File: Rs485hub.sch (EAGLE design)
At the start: 97 parts, among them IC1 SN75176PA, IC2 74AC00N, IC3 SN75176PA, IC4 74AC00N, IC5 SN75176PA, IC6 74AC00N, IC7 SN75176PA, IC8 74AC00N

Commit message: Further mods for the 19" rack at RaumZeitLabor, still needs routing
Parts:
- removed J1, J2, J3, J4: (no value), con-amp:557786-1
- removed RXD1, RXD2, RXD3, RXD4: Grn rxd, led:LED3MM
- removed TXD1, TXD2, TXD3, TXD4: red txd, led:LED3MM
- added U$2, U$3, U$4, U$5: RJHS508, RJHS:RJHS508
- added X1: MAB64, con-vg:MAB64
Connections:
- net GND: now also U$2G$2.PK$1, U$2G$3.PK$1, U$3G$2.PK$1, U$3G$3.PK$1, U$4G$2.PK$1, U$4G$3.PK$1, U$5G$2.PK$1, U$5G$3.PK$1, X1A.29; no longer RXD1.C, RXD2.C, RXD3.C, RXD4.C, TXD1.C, TXD2.C, TXD3.C, TXD4.C
- net N$1: now also U$2G$3.PA$1; no longer TXD1.A
- net N$10: now also U$2G$1.P$1; no longer J2.1
- net N$17: now also U$3G$2.PA$1; no longer RXD2.A
- net N$18: now also U$3G$1.P$2; no longer J3.2
- net N$2: now also U$2G$2.PA$1; no longer RXD1.A
- net N$20: now also U$3G$1.P$1; no longer J3.1
- net N$21: now also U$5G$1.P$1; no longer J1.1
- net N$3: now also U$2G$1.P$7; no longer J2.7
- net N$30: now also U$3G$1.P$7; no longer J3.7
- net N$31: now also U$4G$3.PA$1; no longer TXD3.A
- net N$32: now also U$4G$2.PA$1; no longer RXD3.A
- net N$33: now also U$4G$1.P$2; no longer J4.2
- net N$35: now also U$4G$1.P$1; no longer J4.1
- net N$4: now also U$2G$1.P$2; no longer J2.2
- net N$45: now also U$4G$1.P$7; no longer J4.7
- net N$46: now also U$5G$3.PA$1; no longer TXD4.A
- net N$47: now also U$5G$2.PA$1; no longer RXD4.A
- net N$48: now also U$5G$1.P$2; no longer J1.2
- net N$6: now also U$3G$3.PA$1; no longer TXD2.A
- net N$60: now also U$5G$1.P$7; no longer J1.7
- net VCC: now also X1A.1, X1A.32

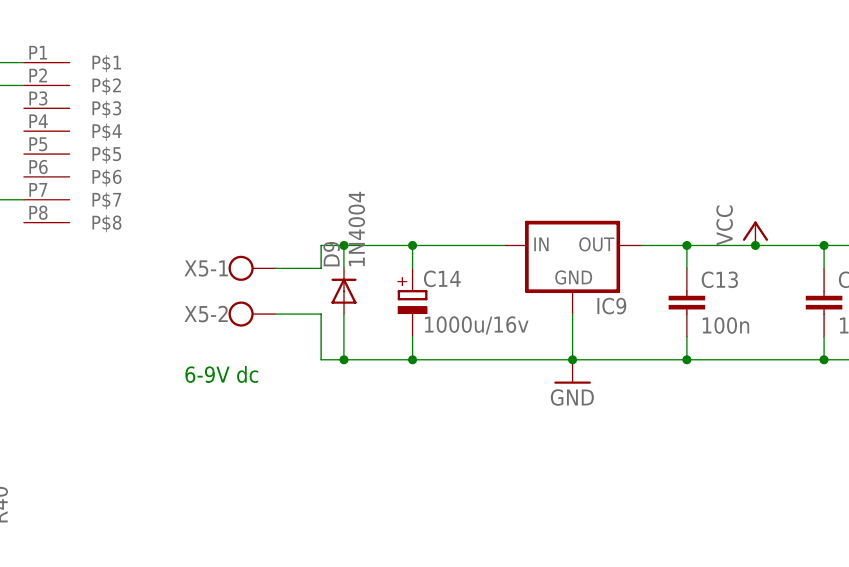
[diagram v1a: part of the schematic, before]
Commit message: Added routing ;)
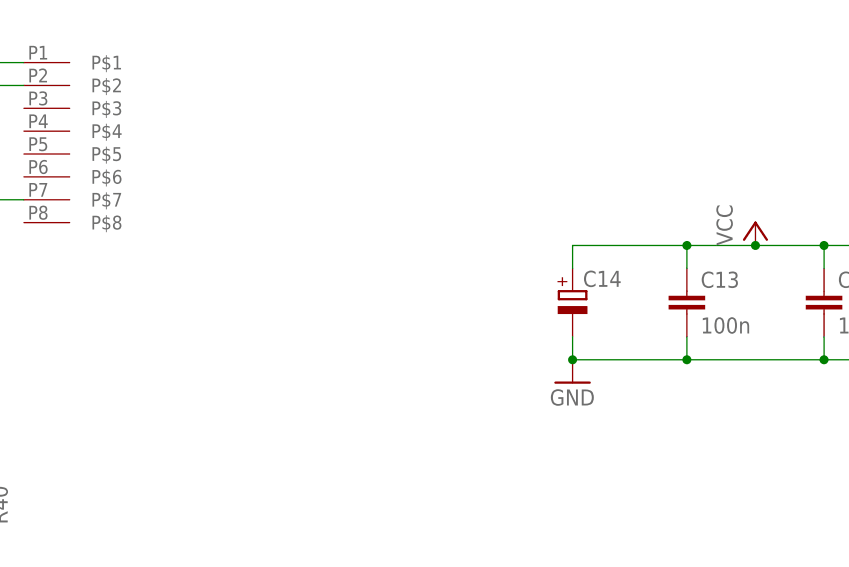
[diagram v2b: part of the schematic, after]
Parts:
- removed D9: 1N4004, diode:1N4004
- removed IC9: (no value), v-reg:78XXS
- removed X5: (no value), con-wago-500:W237-102
- C14: value 1000u/16v -> (none); device rcl:CPOL-EUE5-13 -> rcl:CPOL-EUE5-8.5
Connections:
- removed net N$7: C14.+, D9.C, IC9.IN, X5-1.KL
- net GND: no longer D9.A, IC9.GND, X5-2.KL
- net VCC: now also C14.+; no longer IC9.OUT
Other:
- note removed: "6-9V dc"
- moved on the sheet: C14
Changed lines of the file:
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@@
 <part name="C12" library="capacitor-wima" deviceset="C" device="2,5-3" value="100n"/>
 <part name="R41" library="rcl" deviceset="R-EU_" device="0309/10" value="2k2"/>
-<part name="X5" library="con-wago-500" deviceset="W237-102" device=""/>
-<part name="IC9" library="v-reg" deviceset="78XXS" device=""/>
-<part name="D9" library="diode" deviceset="1N4004" device=""/>
 <part name="C13" library="capacitor-wima" deviceset="C" device="2,5-3" value="100n"/>
-<part name="C14" library="rcl" deviceset="CPOL-EU" device="E5-13" value="1000u/16v"/>
 <part name="STACK" library="con-lstb" deviceset="MA03-1" device=""/>
 <part name="P+5" library="supply1" deviceset="VCC" device=""/>
@@
 <part name="U$4" library="RJHS" deviceset="RJHS508" device=""/>
 <part name="U$5" library="RJHS" deviceset="RJHS508" device=""/>
+<part name="C14" library="rcl" deviceset="CPOL-EU" device="E5-8.5"/>
 </parts>
 <sheets>
@@
 <text x="96.52" y="144.78" size="1.778" layer="91">Terminate</text>
 <text x="20.32" y="121.92" size="1.778" layer="91">Rxen</text>
-<text x="127" y="81.28" size="1.778" layer="91">6-9V dc</text>
 <text x="294.64" y="121.92" size="1.778" layer="91">Expantion</text>
 </plain>
@@
 <instance part="C12" gate="G$1" x="269.24" y="91.44"/>
 <instance part="R41" gate="G$1" x="10.16" y="241.3" rot="R90"/>
-<instance part="X5" gate="-1" x="132.08" y="93.98"/>
-<instance part="X5" gate="-2" x="132.08" y="88.9"/>
-<instance part="IC9" gate="1" x="170.18" y="96.52"/>
-<instance part="D9" gate="1" x="144.78" y="91.44" rot="R90"/>
 <instance part="C13" gate="G$1" x="182.88" y="91.44"/>
-<instance part="C14" gate="G$1" x="152.4" y="91.44"/>
 <instance part="STACK" gate="G$1" x="299.72" y="119.38" rot="R270"/>
 <instance part="P+5" gate="VCC" x="190.5" y="99.06"/>
@@
 <instance part="U$5" gate="G$2" x="33.02" y="53.34" rot="MR0"/>
 <instance part="U$5" gate="G$3" x="45.72" y="53.34" rot="MR0"/>
+<instance part="C14" gate="G$1" x="170.18" y="91.44"/>
 </instances>
 <busses>
@@
 </segment>
 <segment>
-<wire x1="137.16" y1="88.9" x2="142.24" y2="88.9" width="0.1524" layer="91"/>
-<wire x1="142.24" y1="88.9" x2="142.24" y2="83.82" width="0.1524" layer="91"/>
-<wire x1="142.24" y1="83.82" x2="144.78" y2="83.82" width="0.1524" layer="91"/>
-<wire x1="144.78" y1="83.82" x2="152.4" y2="83.82" width="0.1524" layer="91"/>
-<wire x1="152.4" y1="83.82" x2="170.18" y2="83.82" width="0.1524" layer="91"/>
 <wire x1="170.18" y1="83.82" x2="182.88" y2="83.82" width="0.1524" layer="91"/>
 <wire x1="182.88" y1="83.82" x2="198.12" y2="83.82" width="0.1524" layer="91"/>
@@
 <wire x1="218.44" y1="83.82" x2="228.6" y2="83.82" width="0.1524" layer="91"/>
 <wire x1="228.6" y1="83.82" x2="228.6" y2="86.36" width="0.1524" layer="91"/>
-<wire x1="152.4" y1="86.36" x2="152.4" y2="83.82" width="0.1524" layer="91"/>
-<wire x1="170.18" y1="88.9" x2="170.18" y2="83.82" width="0.1524" layer="91"/>
+<wire x1="170.18" y1="86.36" x2="170.18" y2="83.82" width="0.1524" layer="91"/>
 <wire x1="228.6" y1="83.82" x2="238.76" y2="83.82" width="0.1524" layer="91"/>
 <wire x1="238.76" y1="83.82" x2="248.92" y2="83.82" width="0.1524" layer="91"/>
@@
 <wire x1="198.12" y1="86.36" x2="198.12" y2="83.82" width="0.1524" layer="91"/>
 <wire x1="182.88" y1="86.36" x2="182.88" y2="83.82" width="0.1524" layer="91"/>
-<wire x1="144.78" y1="88.9" x2="144.78" y2="83.82" width="0.1524" layer="91"/>
 <wire x1="297.18" y1="111.76" x2="297.18" y2="83.82" width="0.1524" layer="91"/>
-<junction x="144.78" y="83.82"/>
-<junction x="152.4" y="83.82"/>
 <junction x="170.18" y="83.82"/>
 <junction x="182.88" y="83.82"/>
@@
 <junction x="269.24" y="83.82"/>
 <junction x="287.02" y="83.82"/>
-<pinref part="X5" gate="-2" pin="KL"/>
 <pinref part="C8" gate="G$1" pin="2"/>
-<pinref part="C14" gate="G$1" pin="-"/>
-<pinref part="IC9" gate="1" pin="GND"/>
 <pinref part="C12" gate="G$1" pin="2"/>
 <pinref part="C11" gate="G$1" pin="2"/>
@@
 <pinref part="C5" gate="G$1" pin="2"/>
 <pinref part="C13" gate="G$1" pin="2"/>
-<pinref part="D9" gate="1" pin="A"/>
 <pinref part="STACK" gate="G$1" pin="1"/>
 <pinref part="GND5" gate="1" pin="GND"/>
 <pinref part="POWER" gate="G$1" pin="C"/>
+<pinref part="C14" gate="G$1" pin="-"/>
 </segment>
 <segment>
@@
 </segment>
 <segment>
-<wire x1="177.8" y1="96.52" x2="182.88" y2="96.52" width="0.1524" layer="91"/>
 <wire x1="182.88" y1="96.52" x2="190.5" y2="96.52" width="0.1524" layer="91"/>
 <wire x1="190.5" y1="96.52" x2="198.12" y2="96.52" width="0.1524" layer="91"/>
@@
 <junction x="190.5" y="96.52"/>
 <junction x="274.32" y="96.52"/>
-<pinref part="IC9" gate="1" pin="OUT"/>
 <pinref part="C12" gate="G$1" pin="1"/>
 <pinref part="C13" gate="G$1" pin="1"/>
@@
 <pinref part="P+5" gate="VCC" pin="VCC"/>
 <pinref part="R42" gate="G$1" pin="2"/>
+<pinref part="C14" gate="G$1" pin="+"/>
+<wire x1="170.18" y1="93.98" x2="170.18" y2="96.52" width="0.1524" layer="91"/>
+<wire x1="170.18" y1="96.52" x2="182.88" y2="96.52" width="0.1524" layer="91"/>
 </segment>
 <segment>
@@
 </segment>
 </net>
-<net name="N$7" class="1">
-<segment>
-<wire x1="137.16" y1="93.98" x2="142.24" y2="93.98" width="0.1524" layer="91"/>
-<wire x1="142.24" y1="93.98" x2="142.24" y2="96.52" width="0.1524" layer="91"/>
-<wire x1="142.24" y1="96.52" x2="144.78" y2="96.52" width="0.1524" layer="91"/>
-<wire x1="144.78" y1="96.52" x2="152.4" y2="96.52" width="0.1524" layer="91"/>
-<wire x1="152.4" y1="96.52" x2="162.56" y2="96.52" width="0.1524" layer="91"/>
-<wire x1="144.78" y1="93.98" x2="144.78" y2="96.52" width="0.1524" layer="91"/>
-<wire x1="152.4" y1="93.98" x2="152.4" y2="96.52" width="0.1524" layer="91"/>
-<junction x="144.78" y="96.52"/>
-<junction x="152.4" y="96.52"/>
-<pinref part="X5" gate="-1" pin="KL"/>
-<pinref part="IC9" gate="1" pin="IN"/>
-<pinref part="D9" gate="1" pin="C"/>
-<pinref part="C14" gate="G$1" pin="+"/>
-</segment>
-</net>
